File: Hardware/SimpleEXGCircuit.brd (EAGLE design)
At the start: 38.1 x 38.1 mm, 27 parts

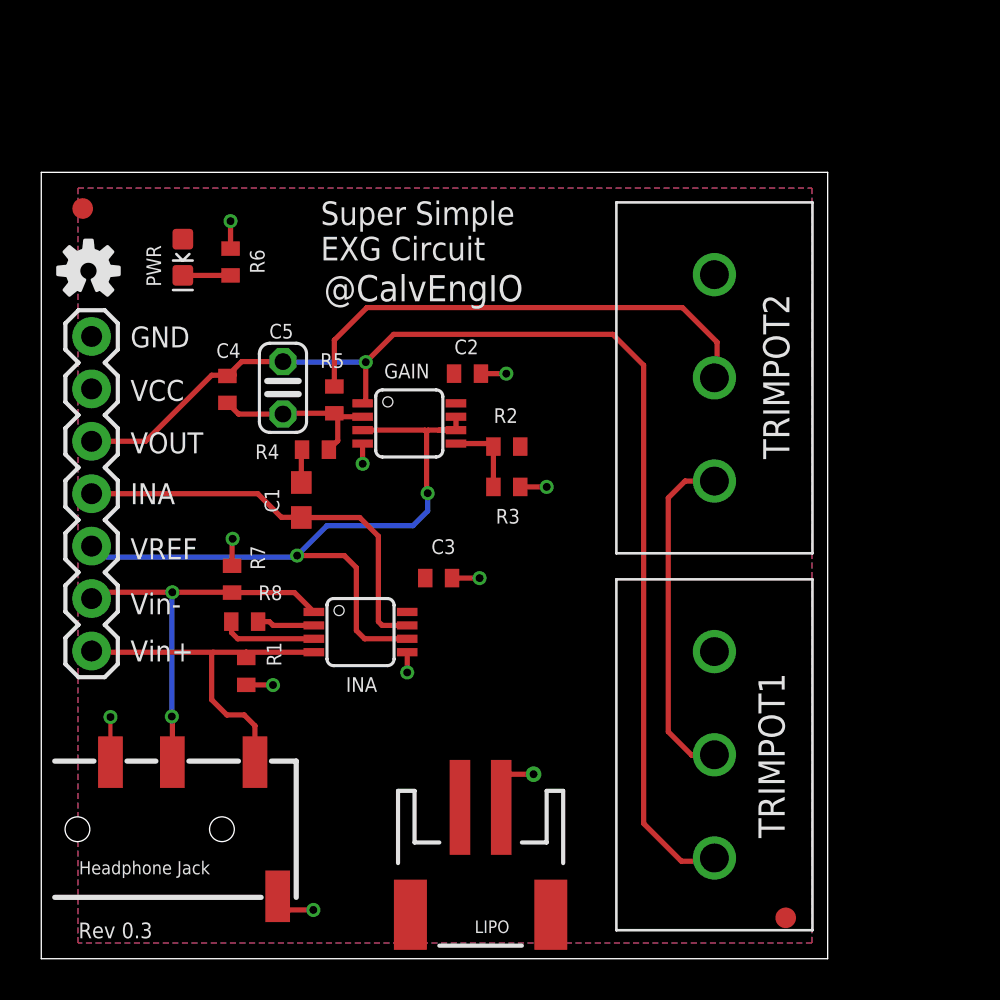
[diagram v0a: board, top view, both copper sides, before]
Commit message: new hardware design with optoisolator and coin cell battery
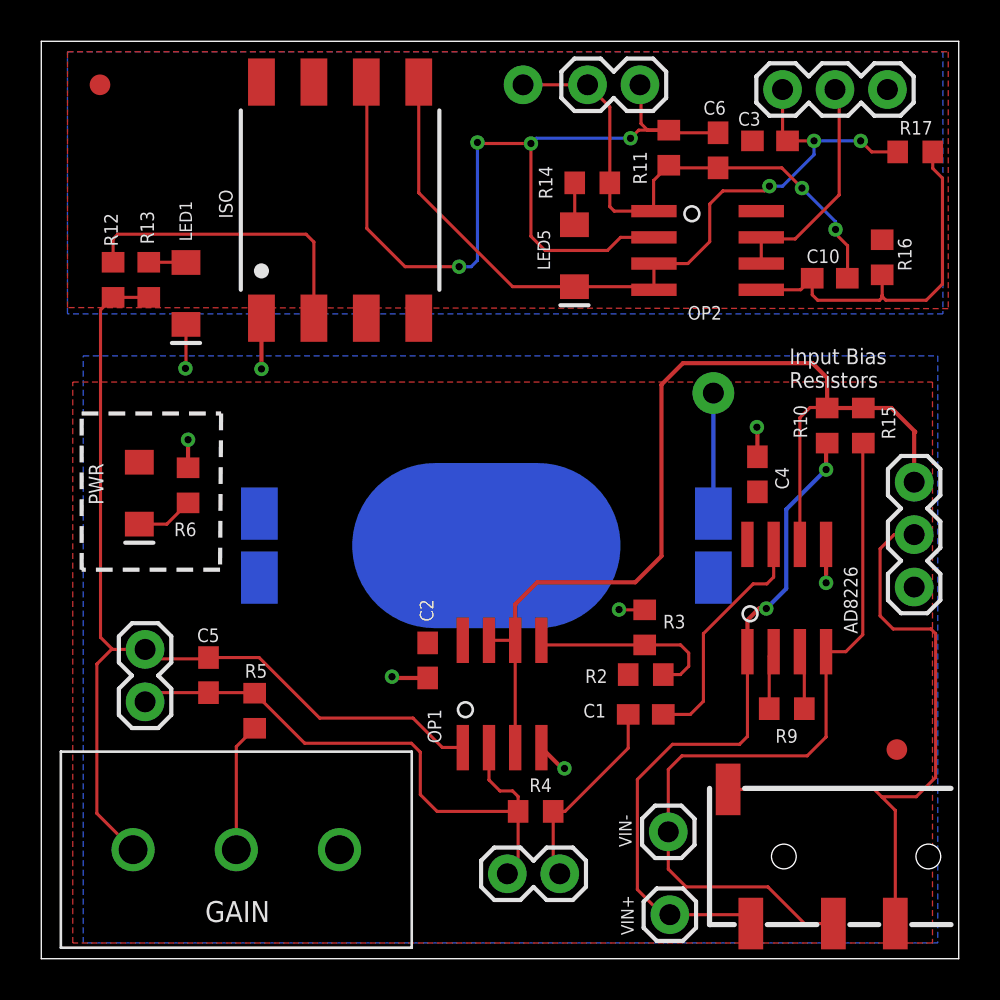
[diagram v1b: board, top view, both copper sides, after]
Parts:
- removed INA: INA-B, CalvEngIO-AnalogIC:MSOP08
- removed JP1: (no value), SparkFun-Connectors:1X07
- removed LIPO: (no value), CalvEngIO-Connectors:JST-2-SMD
- removed R1, R7: xk, CalvEngIO-Passives:R0402
- removed R8: 1k, CalvEngIO-Passives:R0402
- removed TRIMPOT1, TRIMPOT2: (no value), CalvEngIO-Passives:16MMROTARYPOT
- removed U$2, U$3: FIDUCIAL, CalvEngIO-Connectors:FIDUCIAL_1MM
- added AD8226: INA-ASO8, CalvEngIO-AnalogIC:SO8
- added BT1: (no value), CalvEngIO-Connectors:BATTCON_20MM_4LEGS_OVERPASTE
- added C10: 2.2u, CalvEngIO-Passives:C0603
- added C6: 820p, CalvEngIO-Passives:C0603
- added ISO: HCNR200-300E, avago:DIP8-400
- added J1, J2, J6: (no value), CalvEngIO-Connectors:1X02
- added J4, J7: (no value), CalvEngIO-Connectors:1X03
- added J5: (no value), CalvEngIO-Connectors:1X01NS_KIT
- added LED1, LED5: (no value), CalvEngIO-LED:LED-1206
- added LOGO4: OSHW-LOGOL, CalvEngIO-Logos:OSHW-LOGO-L
- added OP, OP2: (no value), CalvEngIO-AnalogIC:SO8
- added R10, R15: (no value), CalvEngIO-Passives:R0603
- added R11: 200k, CalvEngIO-Passives:R0603
- added R12, R13, R14: 806, CalvEngIO-Passives:R0603
- added R16: 154k, CalvEngIO-Passives:R0603
- added R17: 287k, CalvEngIO-Passives:R0603
- added R9: 1k, CalvEngIO-Passives:R0603
- added VIN+, VIN-: (no value), CalvEngIO-Connectors:1X01
- C1: value 2.2u -> 4.7u
- C2: device CalvEngIO-Passives:C0402 -> CalvEngIO-Passives:C0603
- C3: value 100n -> 2.2u; device CalvEngIO-Passives:C0402 -> CalvEngIO-Passives:C0603
- C4: value 680p -> 100n; device CalvEngIO-Passives:C0402 -> CalvEngIO-Passives:C0603
- C5: value xF -> 150p; device resistor:C025-024X044 -> CalvEngIO-Passives:C0603
- GAIN: value OP-DUALRM -> (none); device CalvEngIO-AnalogIC:MSOP08 -> CalvEngIO-Passives:16MMROTARYPOT
- LOGO1: value OSHW-LOGOS -> REVISION.C; device SparkFun-Aesthetics:OSHW-LOGO-S -> CalvEngIO-Logos:REV.C
- PWR: device CalvEngIO-LED:LED-0603 -> CalvEngIO-LED:LED-1206
- R2, R3, R6: device CalvEngIO-Passives:R0402 -> CalvEngIO-Passives:R0603
- R4: value 100k -> 50k; device CalvEngIO-Passives:R0402 -> CalvEngIO-Passives:R0603
- R5: value 100k -> 1M; device CalvEngIO-Passives:R0402 -> CalvEngIO-Passives:R0603
- U$4: value WEBSITE.05 -> CALVENGIO_HANDLEHANDLE.05; device CalvEngIO-Logos:WEBSITE.05 -> CalvEngIO-Logos:CALVENGIO_HANDLE.05
- U$5: value @HANDLE.1 -> FIDUCIAL; device CalvEngIO-Logos:@HANDLE.1 -> CalvEngIO-Connectors:FIDUCIAL_1MM
- U$6: value @HANDLE.05 -> FIDUCIAL; device CalvEngIO-Logos:@HANDLE.05 -> CalvEngIO-Connectors:FIDUCIAL_1MM
- moved U$1 44.4 mm to (44.6, 4.95), turned to 180 degrees
- moved U$6 31.4 mm to (41.5, 10.1)
- moved C3 26.6 mm to (35.3, 39.6), turned to 180 degrees
- moved C4 26.0 mm to (34.7, 23.5)
- moved GAIN 22.3 mm to (9.45, 5.28), turned to 180 degrees
- moved R4 20.5 mm to (24.0, 7.14), turned to 0 degrees
- moved U$4 20.4 mm to (37.1, 34.1)
- moved C1 19.7 mm to (29.3, 11.8), turned to 180 degrees
- moved U$5 16.7 mm to (2.84, 42.3), flipped to the top
- moved R5 15.5 mm to (10.3, 12.0), turned to 90 degrees
- moved C5 14.4 mm to (8.10, 13.7)
- moved C2 14.0 mm to (18.7, 14.5), turned to 90 degrees
- moved R2 12.9 mm to (29.3, 13.8), turned to 180 degrees
- moved PWR 11.6 mm to (4.75, 22.6)
- moved R6 11.0 mm to (7.11, 22.9)
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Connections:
- removed net GND: C2.1, C3.2, GAIN.4, INA.5, JP1.7, LIPO.1, R1.1, R3.1, R6.1, R7.1, U$1.EARTH, U$1.RING2
- removed net N$4: C1.2, R4.2
- removed net OUT: C4.2, C5.2, GAIN.1, JP1.5, TRIMPOT1.3
- removed net VCC: C2.2, C3.1, GAIN.8, INA.8, JP1.6, LIPO.2, PWR.A, R2.2
- new net 5V: C3.2, J7.3, OP2.8, R16.2
- new net AGND: AD8226.5, BT1.2, C2.1, C4.2, ISO.1, J4.1, LED1.C, OP.4, R3.1, R6.1
- new net CH2: C10.1, C6.2, J5.1, J6.2, OP2.1, R11.1, R14.2
- new net DGND: C3.1, ISO.5, J7.1, LED5.C, OP2.3, OP2.4, R17.1
- new net EXG: C5.2, GAIN.3, J2.2, OP.1, R12.2, R13.2
- new net EXG_ISO: J7.2, OP2.6, OP2.7
- new net N$10: C6.1, ISO.6, J6.1, OP2.2, R11.2
- new net N$11: ISO.2, R12.1
- new net N$12: C10.2, OP2.5, R16.1, R17.2
- new net N$17: LED1.A, R13.1
- new net N$19: LED5.A, R14.1
- new net VCOIN: AD8226.8, BT1.1, C2.2, C4.1, OP.8, PWR.A, R2.2
- new net VIN-REF: J4.2, U$1.EARTH, U$1.RING2
- net INA: now also AD8226.7; no longer INA.7, JP1.4
- net N$1: now also GAIN.2; no longer TRIMPOT2.2
- net N$2: now also AD8226.2, R9.2; no longer TRIMPOT1.2, TRIMPOT2.3
- net N$3: now also OP.5; no longer GAIN.5
- net N$5: now also J1.2, J2.1, OP.2; no longer C4.1, GAIN.2
- net N$7: now also AD8226.3, R9.1; no longer INA.2, R8.1
- net N$8: now also C1.2, J1.1, R4.2; no longer INA.3, R8.2
- net VIN+: now also AD8226.1, R10.2, VIN+.1; no longer INA.4, JP1.1, R1.2
- net VIN-: now also AD8226.4, R15.2, VIN-.1; no longer INA.1, JP1.2, R7.2
- net VREF: now also AD8226.6, J4.3, OP.3, OP.6, OP.7, R10.1, R15.1; no longer GAIN.3, GAIN.6, GAIN.7, INA.6, JP1.3
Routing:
- net OUT: track 58.4 -> 0.00 mm, vias 1 -> 0
- net EXG: track 0.00 -> 49.2 mm
- net N$10: track 0.00 -> 45.5 mm, vias 0 -> 4
- net DGND: track 0.00 -> 39.8 mm, vias 0 -> 3
- net VIN-REF: track 0.00 -> 32.2 mm
- net CH2: track 0.00 -> 26.4 mm, vias 0 -> 2
- net N$5: track 8.63 -> 29.1 mm
- net N$12: track 0.00 -> 18.1 mm
- net VIN-: track 20.0 -> 37.9 mm, vias 2 -> 0
- net N$1: track 23.9 -> 6.25 mm
- net GND: track 17.0 -> 0.00 mm, vias 11 -> 0
- net VIN+: track 17.8 -> 33.9 mm, vias 0 -> 2
- net N$11: track 0.00 -> 14.8 mm
- net AGND: track 0.00 -> 14.7 mm, vias 0 -> 8
- net N$2: track 16.6 -> 2.85 mm
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- added copper zone on layer 1, net 5V
- added copper zone on layer 16, net AGND
- added copper zone on layer 16, net DGND
- added copper zone on layer 1, net VCOIN
- removed copper zone on layer 16, net GND
- removed copper zone on layer 1, net VCC
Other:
- board size 38.1 x 38.1 mm -> 44.5 x 44.5 mm
- board text added: "5V"
- board text added: "AD8226"
- board text added: "DGND"
- board text added: "EREF"
- board text added: "Input Bias Resistors"
- board text added: "OP1"
- board text added: "OUT"
- board text removed: "Creative Commons License Attribution-ShareAlike 4.0 Unported CC BY-SA-4.0"
- board text removed: "Headphone Jack"
- board text removed: "INA"
- board text removed: "Rev 0.3"
- board text removed: "VCC"
- board text removed: "VOUT"
- board text removed: "Vin+"
- board text removed: "Vin-"
